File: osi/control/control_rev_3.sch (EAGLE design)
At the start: 9 parts

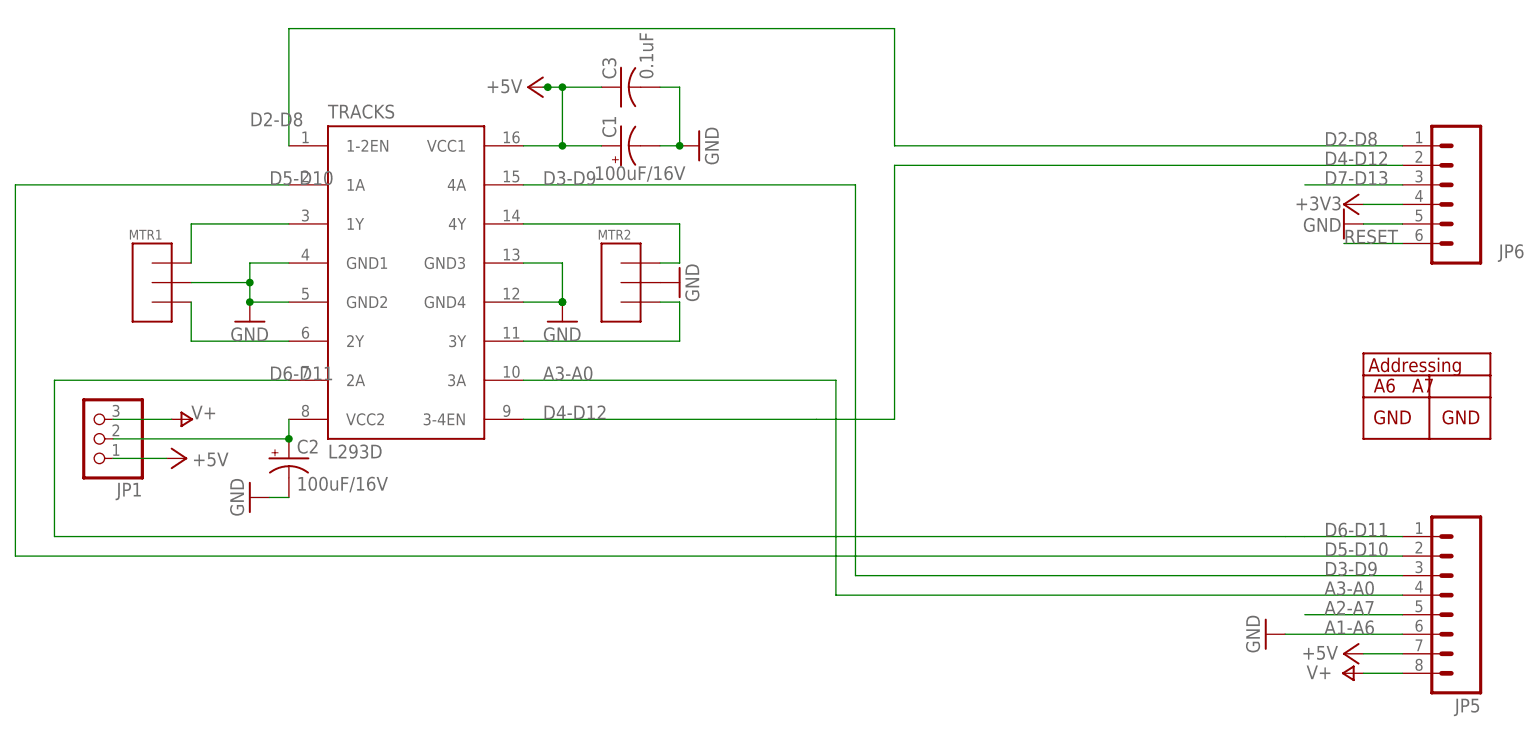
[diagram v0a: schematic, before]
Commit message: moving headers
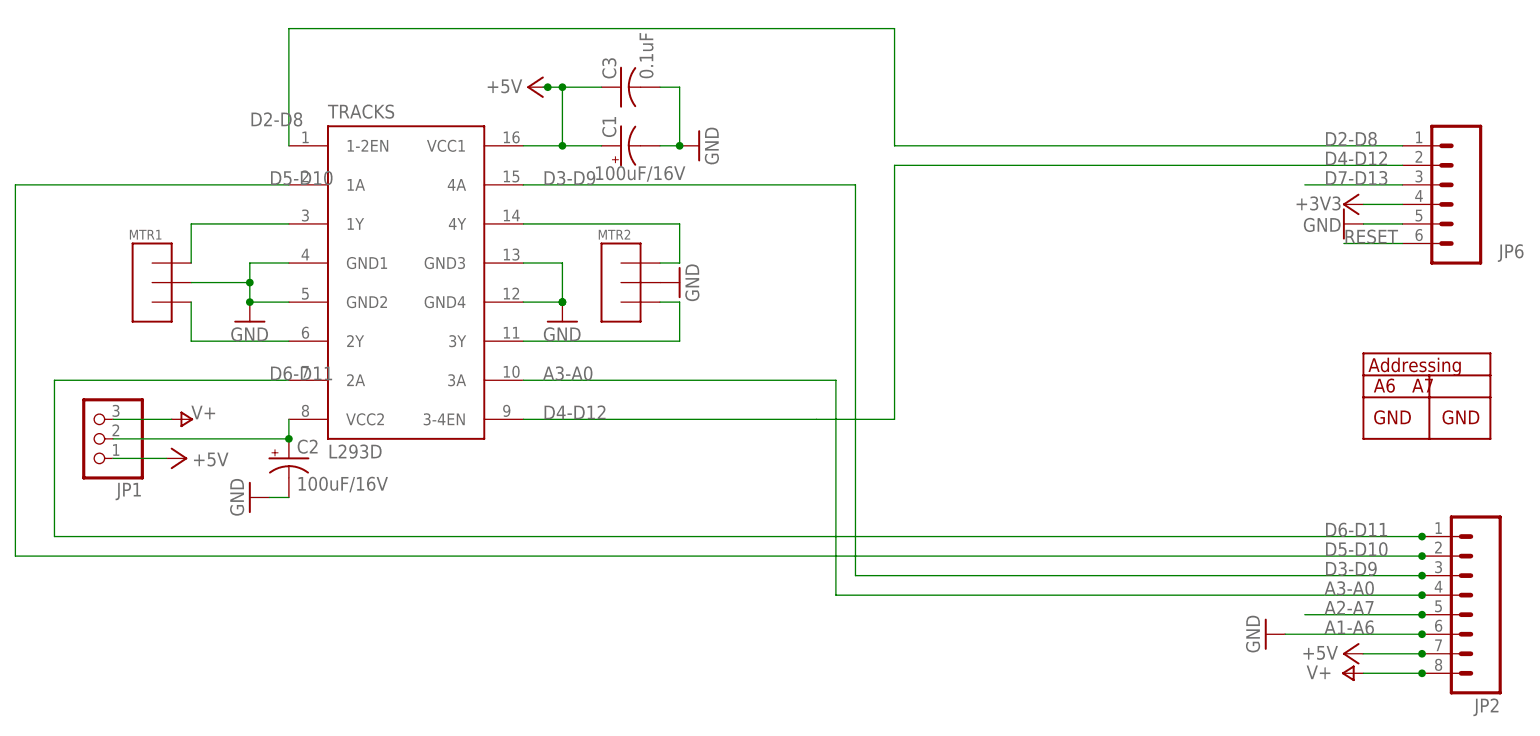
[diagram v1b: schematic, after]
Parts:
- removed JP5: (no value), SparkFun_mod:M081X08
- added JP2: (no value), SparkFun:M081X08
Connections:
- net +5V: now also JP2.7; no longer JP5.7
- net A1-A6: now also JP2.6; no longer JP5.6
- net A2-A7: now also JP2.5; no longer JP5.5
- net A3-A0: now also JP2.4; no longer JP5.4
- net D3-D9: now also JP2.3; no longer JP5.3
- net D5-D10: now also JP2.2; no longer JP5.2
- net D6-D11: now also JP2.1; no longer JP5.1
- net V+: now also JP2.8; no longer JP5.8
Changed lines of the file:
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@@
 <part name="JP6" library="SparkFun" deviceset="M06" device="SIP"/>
 <part name="FRAME1" library="SparkFun_mod" deviceset="FRAME-LETTER" device=""/>
-<part name="JP5" library="SparkFun_mod" deviceset="M08" device="1X08"/>
 <part name="TRACKS" library="texas" deviceset="L293E" device="" value="L293D"/>
 <part name="GND12" library="supply1" deviceset="GND" device=""/>
@@
 <part name="GND" library="_my-parts" deviceset="ADDRESSING" device="" value="GND"/>
 <part name="GND2" library="supply1" deviceset="GND" device=""/>
+<part name="JP2" library="SparkFun" deviceset="M08" device="1X08"/>
 </parts>
 <sheets>
@@
 <instance part="FRAME1" gate="G$1" x="-73.66" y="-30.48"/>
 <instance part="FRAME1" gate="G$2" x="73.66" y="-30.48"/>
-<instance part="JP5" gate="G$1" x="132.08" y="30.48" rot="R180"/>
 <instance part="TRACKS" gate="G$1" x="-2.54" y="71.12"/>
 <instance part="GND12" gate="1" x="-22.86" y="66.04"/>
@@
 <instance part="GND" gate="G$1" x="121.92" y="50.8"/>
 <instance part="GND2" gate="1" x="109.22" y="25.4" rot="R270"/>
+<instance part="JP2" gate="G$1" x="134.62" y="30.48" rot="R180"/>
 </instances>
 <busses>
@@
 <net name="V+" class="0">
 <segment>
-<pinref part="JP5" gate="G$1" pin="8"/>
 <pinref part="P+2" gate="1" pin="V+"/>
-<wire x1="127" y1="20.32" x2="121.92" y2="20.32" width="0.1524" layer="91"/>
+<wire x1="129.54" y1="20.32" x2="121.92" y2="20.32" width="0.1524" layer="91"/>
+<pinref part="JP2" gate="G$1" pin="8"/>
+<junction x="129.54" y="20.32"/>
 </segment>
 <segment>
@@
 <net name="+5V" class="0">
 <segment>
-<pinref part="JP5" gate="G$1" pin="7"/>
 <pinref part="P+3" gate="1" pin="+5V"/>
-<wire x1="127" y1="22.86" x2="121.92" y2="22.86" width="0.1524" layer="91"/>
+<wire x1="129.54" y1="22.86" x2="121.92" y2="22.86" width="0.1524" layer="91"/>
+<pinref part="JP2" gate="G$1" pin="7"/>
+<junction x="129.54" y="22.86"/>
 </segment>
 <segment>
@@
 <net name="D6-D11" class="0">
 <segment>
-<pinref part="JP5" gate="G$1" pin="1"/>
-<wire x1="111.76" y1="38.1" x2="114.3" y2="38.1" width="0.1524" layer="91"/>
 <label x="116.84" y="38.1" size="1.778" layer="95"/>
 <pinref part="TRACKS" gate="G$1" pin="2A"/>
-<wire x1="114.3" y1="38.1" x2="127" y2="38.1" width="0.1524" layer="91"/>
 <wire x1="-17.78" y1="58.42" x2="-48.26" y2="58.42" width="0.1524" layer="91"/>
 <wire x1="-48.26" y1="58.42" x2="-48.26" y2="38.1" width="0.1524" layer="91"/>
-<wire x1="-48.26" y1="38.1" x2="111.76" y2="38.1" width="0.1524" layer="91"/>
+<wire x1="-48.26" y1="38.1" x2="129.54" y2="38.1" width="0.1524" layer="91"/>
 <label x="-20.32" y="58.42" size="1.778" layer="95"/>
+<pinref part="JP2" gate="G$1" pin="1"/>
+<junction x="129.54" y="38.1"/>
 </segment>
 </net>
 <net name="D5-D10" class="0">
 <segment>
-<pinref part="JP5" gate="G$1" pin="2"/>
 <label x="116.84" y="35.56" size="1.778" layer="95"/>
 <pinref part="TRACKS" gate="G$1" pin="1A"/>
 <wire x1="-17.78" y1="83.82" x2="-53.34" y2="83.82" width="0.1524" layer="91"/>
 <wire x1="-53.34" y1="83.82" x2="-53.34" y2="35.56" width="0.1524" layer="91"/>
-<wire x1="-53.34" y1="35.56" x2="127" y2="35.56" width="0.1524" layer="91"/>
+<wire x1="-53.34" y1="35.56" x2="129.54" y2="35.56" width="0.1524" layer="91"/>
 <label x="-20.32" y="83.82" size="1.778" layer="95"/>
+<pinref part="JP2" gate="G$1" pin="2"/>
+<junction x="129.54" y="35.56"/>
 </segment>
 </net>
 <net name="D3-D9" class="0">
 <segment>
-<pinref part="JP5" gate="G$1" pin="3"/>
 <label x="116.84" y="33.02" size="1.778" layer="95"/>
-<wire x1="127" y1="33.02" x2="55.88" y2="33.02" width="0.1524" layer="91"/>
+<wire x1="129.54" y1="33.02" x2="55.88" y2="33.02" width="0.1524" layer="91"/>
 <wire x1="55.88" y1="33.02" x2="55.88" y2="83.82" width="0.1524" layer="91"/>
 <pinref part="TRACKS" gate="G$1" pin="4A"/>
 <wire x1="55.88" y1="83.82" x2="12.7" y2="83.82" width="0.1524" layer="91"/>
 <label x="15.24" y="83.82" size="1.778" layer="95"/>
+<pinref part="JP2" gate="G$1" pin="3"/>
+<junction x="129.54" y="33.02"/>
 </segment>
 </net>
 <net name="A3-A0" class="0">
 <segment>
-<pinref part="JP5" gate="G$1" pin="4"/>
 <label x="116.84" y="30.48" size="1.778" layer="95"/>
-<wire x1="127" y1="30.48" x2="53.34" y2="30.48" width="0.1524" layer="91"/>
+<wire x1="129.54" y1="30.48" x2="53.34" y2="30.48" width="0.1524" layer="91"/>
 <wire x1="53.34" y1="30.48" x2="53.34" y2="58.42" width="0.1524" layer="91"/>
 <pinref part="TRACKS" gate="G$1" pin="3A"/>
 <wire x1="53.34" y1="58.42" x2="12.7" y2="58.42" width="0.1524" layer="91"/>
 <label x="15.24" y="58.42" size="1.778" layer="95"/>
+<pinref part="JP2" gate="G$1" pin="4"/>
+<junction x="129.54" y="30.48"/>
 </segment>
 </net>
 <net name="A2-A7" class="0">
 <segment>
-<pinref part="JP5" gate="G$1" pin="5"/>
-<wire x1="114.3" y1="27.94" x2="127" y2="27.94" width="0.1524" layer="91"/>
+<wire x1="114.3" y1="27.94" x2="129.54" y2="27.94" width="0.1524" layer="91"/>
 <label x="116.84" y="27.94" size="1.778" layer="95"/>
+<pinref part="JP2" gate="G$1" pin="5"/>
+<junction x="129.54" y="27.94"/>
 </segment>
 </net>
 <net name="A1-A6" class="0">
 <segment>
-<pinref part="JP5" gate="G$1" pin="6"/>
-<wire x1="111.76" y1="25.4" x2="127" y2="25.4" width="0.1524" layer="91"/>
+<wire x1="111.76" y1="25.4" x2="129.54" y2="25.4" width="0.1524" layer="91"/>
 <label x="116.84" y="25.4" size="1.778" layer="95"/>
 <pinref part="GND2" gate="1" pin="GND"/>
-</segment>
-</net>
+<pinref part="JP2" gate="G$1" pin="6"/>
+<junction x="129.54" y="25.4"/>
+</segment>
+</net>
